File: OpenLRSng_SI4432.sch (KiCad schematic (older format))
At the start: 36 parts, among them IC1 ATMEGA328P-A, IC2 Si4432, P1 CONN_01X06, P2 CONN_02X09, P3 MML, U1 MIC5205 3,3V, Y1 RESONATEUR

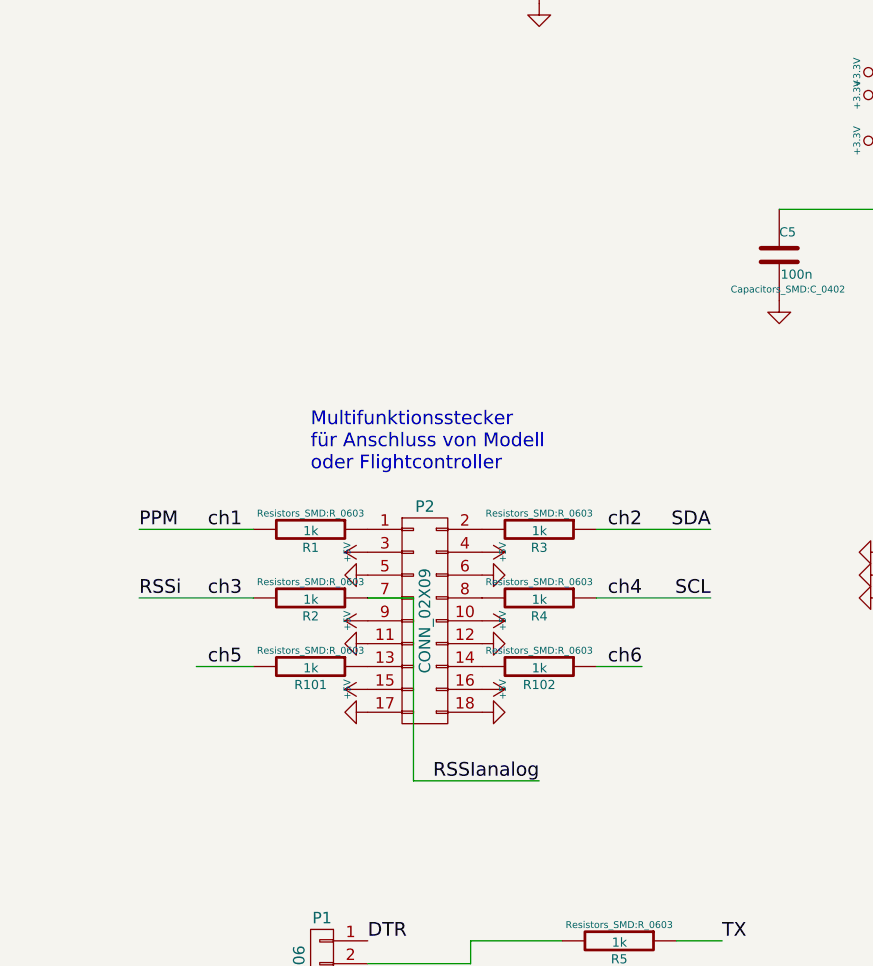
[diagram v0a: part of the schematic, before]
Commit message: Von 6 auf 4 Kanäle reduziert, I2C oder Analog in der Zusätzliche Kanäle über PicoBlade, Spannungsteiler/Pullup/Schutzwiderstandspads
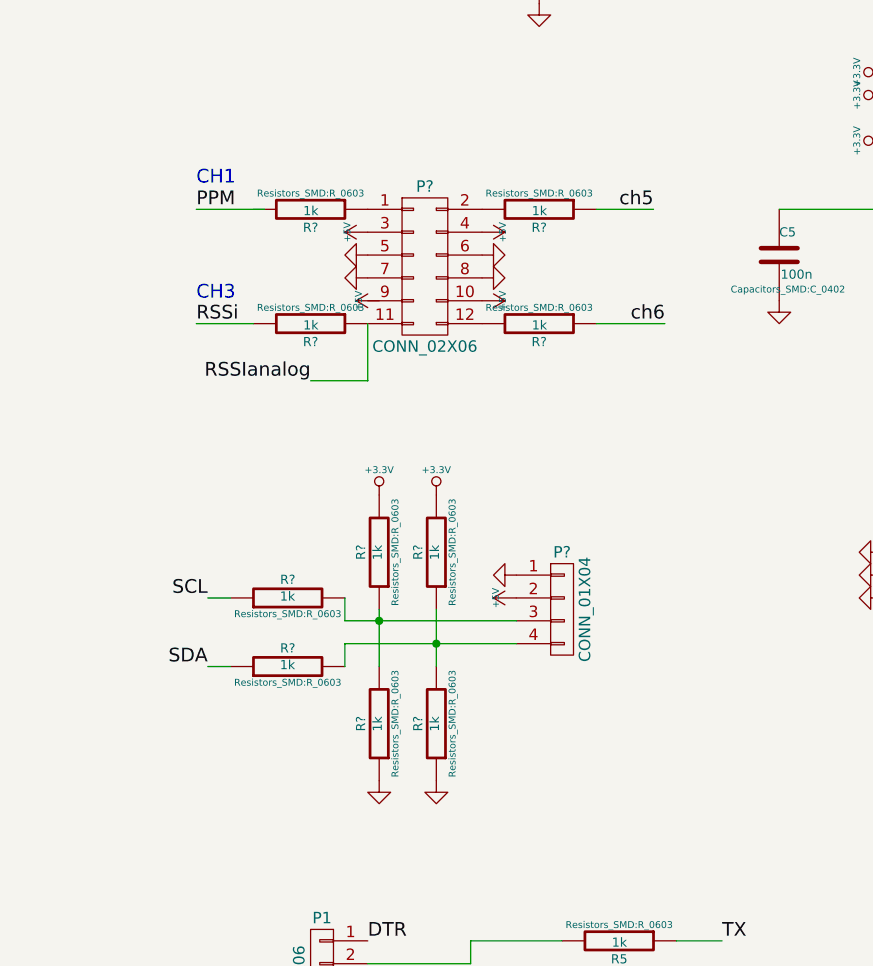
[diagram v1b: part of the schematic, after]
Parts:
- removed P2: CONN_02X09, Pin_Headers:Pin_Header_Angled_2x09, symbol CONN_02X09
- removed R1, R101, R102, R2, R3, R4: 1k, Resistors_SMD:R_0603, symbol R
- added P?: CONN_02X06, symbol CONN_02X06
- added P?: CONN_01X04, symbol CONN_01X04
- added R? (x10): 1k, Resistors_SMD:R_0603, symbol R
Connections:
- net +3.3V: now also R?.2, R?.2
- net +5V: now also P?.10 (P10), P?.2 (P2), P?.3 (P3), P?.4 (P4)
- net GND: now also P?.1 (P1), P?.5 (P5), P?.6 (P6), P?.7 (P7), P?.8 (P8), R?.1, R?.1
- net RSSIanalog: now also P?.11 (P11), R?.1
- net RSSi: now also R?.2
- net SCL: now also R?.1
- net SDA: now also R?.1
- net ch5: now also R?.1
- net ch6: now also R?.1
- new net: P?.1 (P1), R?.1
- new net: P?.12 (P12), R?.2
- new net: P?.2 (P2), R?.2
- new net: P?.3 (P3), R?.1, R?.2, R?.2
- new net: P?.4 (P4), R?.1, R?.2, R?.2
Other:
- note added: "CH1"
- note added: "CH3\n\n"
- note removed: "Multifunktionsstecker\nfür Anschluss von Modell\noder Flightcontroller"

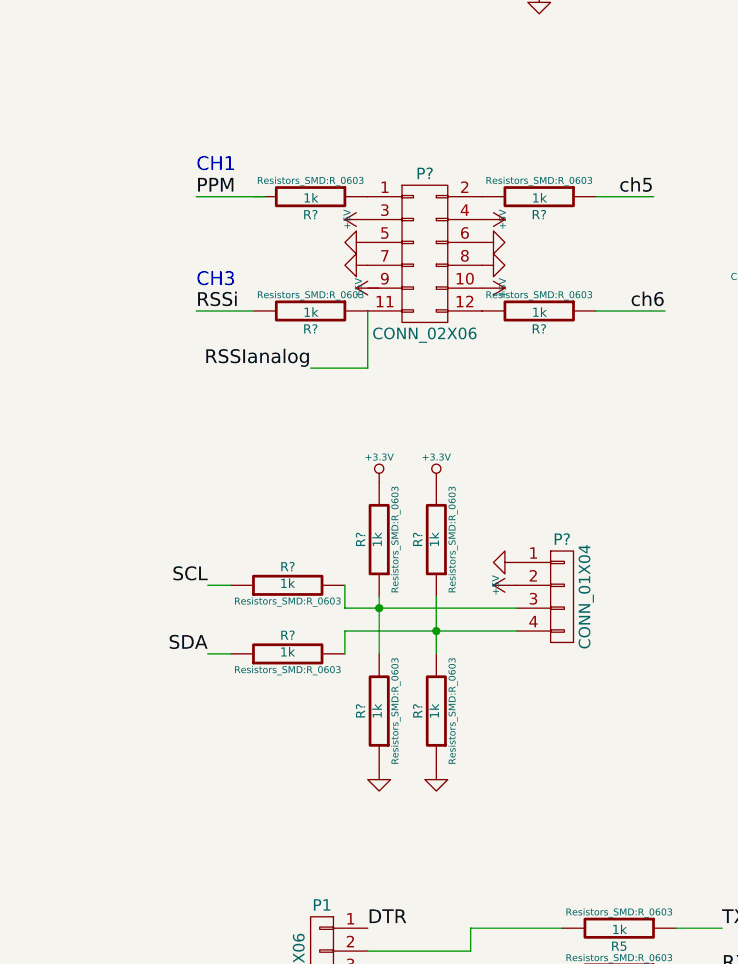
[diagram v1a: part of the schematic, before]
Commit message: Tiefpassfilter Cap an den Analog Inputs nachgerüstet
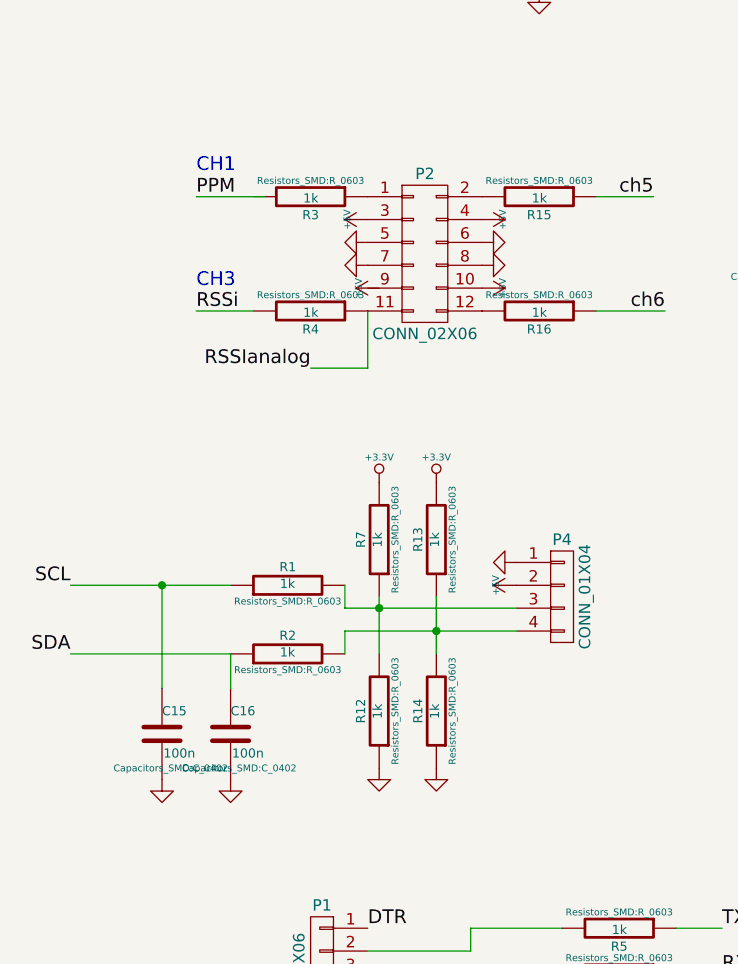
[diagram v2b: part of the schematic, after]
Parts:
- added C15, C16: 100n, Capacitors_SMD:C_0402, symbol C
- gave numbers to parts that had none: 12
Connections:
- net GND: now also C15.2, C16.2
- net SCL: now also C15.1
- net SDA: now also C16.1

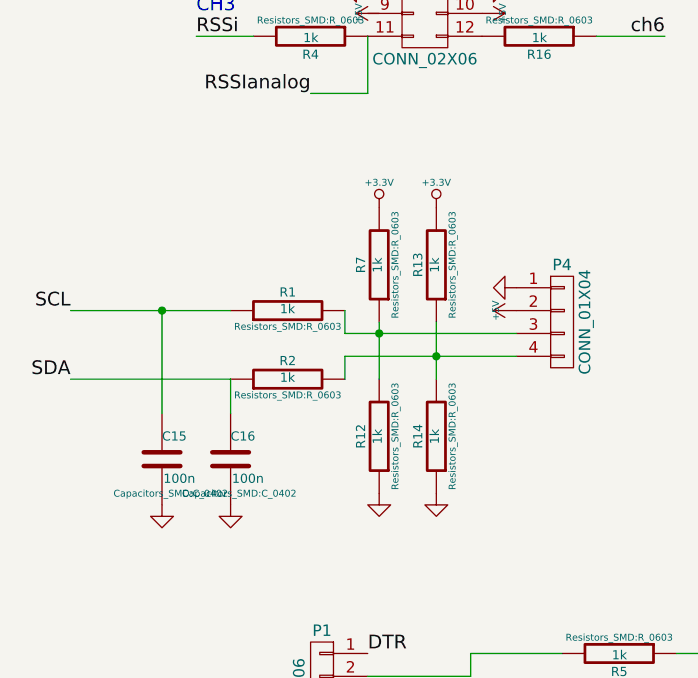
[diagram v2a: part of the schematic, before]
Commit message: Spannungsteiler korrigiert...
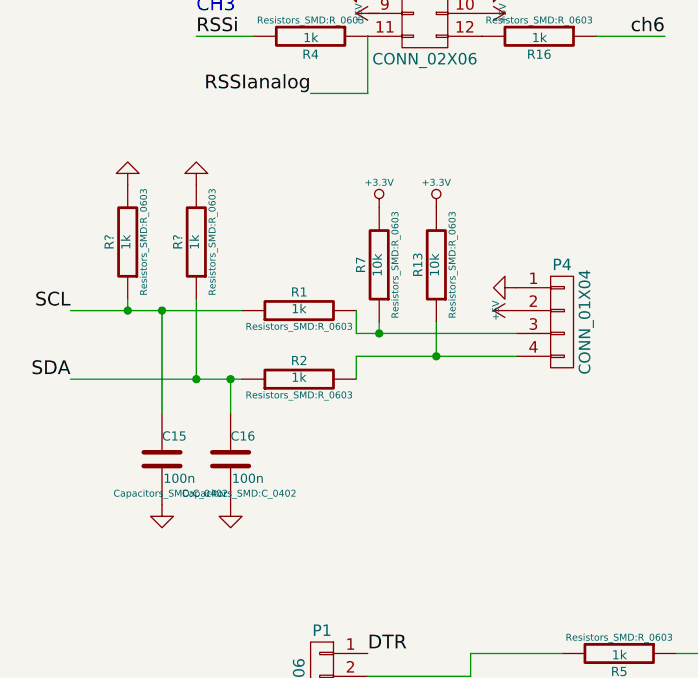
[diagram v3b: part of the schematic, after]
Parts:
- removed R12, R14: 1k, Resistors_SMD:R_0603, symbol R
- added R? (x2): 1k, Resistors_SMD:R_0603, symbol R
- R13, R7: value 1k -> 10k
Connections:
- net GND: now also R?.2, R?.2
- net SCL: now also R?.1
- net SDA: now also R?.1
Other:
- moved on the sheet: R1, R2
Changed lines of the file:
@@
 Text Label 850  5150 2    60   ~ 0
 SDA
-Wire Wire Line
-	2050 4950 2800 4950
-Wire Wire Line
-	2050 5050 2800 5050
 $Comp
 L R R13
@@
 P 2450 4650
 F 0 "R13" V 2530 4650 40  0000 C CNN
-F 1 "1k" V 2457 4651 40  0000 C CNN
+F 1 "10k" V 2457 4651 40  0000 C CNN
 F 2 "Resistors_SMD:R_0603" V 2380 4650 30  0000 C CNN
 F 3 "" H 2450 4650 30  0000 C CNN
@@
 	-1   0    0    1
 $EndComp
-$Comp
-L R R7
-U 1 1 54ED061F
-P 2200 4650
-F 0 "R7" V 2280 4650 40  0000 C CNN
-F 1 "1k" V 2207 4651 40  0000 C CNN
-F 2 "Resistors_SMD:R_0603" V 2130 4650 30  0000 C CNN
-F 3 "" H 2200 4650 30  0000 C CNN
-	1    2200 4650
-	-1   0    0    1
-$EndComp
-Wire Wire Line
-	2200 4900 2200 5150
-Connection ~ 2200 4950
-Wire Wire Line
-	2450 4900 2450 5150
 Connection ~ 2450 5050
-$Comp
-L +3.3V #PWR14
-U 1 1 54ED0C0E
-P 2200 4400
-F 0 "#PWR14" H 2200 4360 30  0001 C CNN
-F 1 "+3.3V" H 2200 4510 30  0000 C CNN
-F 2 "" H 2200 4400 60  0000 C CNN
-F 3 "" H 2200 4400 60  0000 C CNN
-	1    2200 4400
-	1    0    0    -1
-$EndComp
 $Comp
 L +3.3V #PWR16
@@
 L R R1
 U 1 1 54ED13EB
-P 1800 4850
-F 0 "R1" V 1880 4850 40  0000 C CNN
-F 1 "1k" V 1807 4851 40  0000 C CNN
-F 2 "Resistors_SMD:R_0603" V 1730 4850 30  0000 C CNN
-F 3 "" H 1800 4850 30  0000 C CNN
-	1    1800 4850
+P 1850 4850
+F 0 "R1" V 1930 4850 40  0000 C CNN
+F 1 "1k" V 1857 4851 40  0000 C CNN
+F 2 "Resistors_SMD:R_0603" V 1780 4850 30  0000 C CNN
+F 3 "" H 1850 4850 30  0000 C CNN
+	1    1850 4850
 	0    -1   -1   0
 $EndComp
@@
 L R R2
 U 1 1 54ED1487
-P 1800 5150
-F 0 "R2" V 1880 5150 40  0000 C CNN
-F 1 "1k" V 1807 5151 40  0000 C CNN
-F 2 "Resistors_SMD:R_0603" V 1730 5150 30  0000 C CNN
-F 3 "" H 1800 5150 30  0000 C CNN
-	1    1800 5150
+P 1850 5150
+F 0 "R2" V 1930 5150 40  0000 C CNN
+F 1 "1k" V 1857 5151 40  0000 C CNN
+F 2 "Resistors_SMD:R_0603" V 1780 5150 30  0000 C CNN
+F 3 "" H 1850 5150 30  0000 C CNN
+	1    1850 5150
 	0    -1   -1   0
 $EndComp
 Wire Wire Line
-	2050 4950 2050 4850
-Wire Wire Line
-	2050 5050 2050 5150
-$Comp
-L R R12
-U 1 1 54ED1B22
-P 2200 5400
-F 0 "R12" V 2280 5400 40  0000 C CNN
-F 1 "1k" V 2207 5401 40  0000 C CNN
-F 2 "Resistors_SMD:R_0603" V 2130 5400 30  0000 C CNN
-F 3 "" H 2200 5400 30  0000 C CNN
-	1    2200 5400
-	-1   0    0    1
-$EndComp
-$Comp
-L R R14
-U 1 1 54ED1B95
-P 2450 5400
-F 0 "R14" V 2530 5400 40  0000 C CNN
-F 1 "1k" V 2457 5401 40  0000 C CNN
-F 2 "Resistors_SMD:R_0603" V 2380 5400 30  0000 C CNN
-F 3 "" H 2450 5400 30  0000 C CNN
-	1    2450 5400
-	-1   0    0    1
-$EndComp
-Wire Wire Line
-	850  4850 1550 4850
-$Comp
-L GND #PWR15
-U 1 1 54ED1E5C
-P 2200 5650
-F 0 "#PWR15" H 2200 5650 30  0001 C CNN
-F 1 "GND" H 2200 5580 30  0001 C CNN
-F 2 "" H 2200 5650 60  0000 C CNN
-F 3 "" H 2200 5650 60  0000 C CNN
-	1    2200 5650
-	1    0    0    -1
-$EndComp
-$Comp
-L GND #PWR17
-U 1 1 54ED1E97
-P 2450 5650
-F 0 "#PWR17" H 2450 5650 30  0001 C CNN
-F 1 "GND" H 2450 5580 30  0001 C CNN
-F 2 "" H 2450 5650 60  0000 C CNN
-F 3 "" H 2450 5650 60  0000 C CNN
-	1    2450 5650
-	1    0    0    -1
-$EndComp
+	850  4850 1600 4850
 Text Notes 1400 3050 0    60   ~ 0
 CH1
@@
 Connection ~ 1250 4850
 Wire Wire Line
-	850  5150 1550 5150
+	850  5150 1600 5150
 $Comp
 L GND #PWR5
@@
 	1    0    0    -1
 $EndComp
+Connection ~ 2200 4950
+$Comp
+L +3.3V #PWR14
+U 1 1 54ED0C0E
+P 2200 4400
+F 0 "#PWR14" H 2200 4360 30  0001 C CNN
+F 1 "+3.3V" H 2200 4510 30  0000 C CNN
+F 2 "" H 2200 4400 60  0000 C CNN
+F 3 "" H 2200 4400 60  0000 C CNN
+	1    2200 4400
+	1    0    0    -1
+$EndComp
+$Comp
+L R R7
+U 1 1 54ED061F
+P 2200 4650
+F 0 "R7" V 2280 4650 40  0000 C CNN
+F 1 "10k" V 2207 4651 40  0000 C CNN
+F 2 "Resistors_SMD:R_0603" V 2130 4650 30  0000 C CNN
+F 3 "" H 2200 4650 30  0000 C CNN
+	1    2200 4650
+	-1   0    0    1
+$EndComp
+Wire Wire Line
+	2200 4950 2200 4900
+Wire Wire Line
+	2450 5050 2450 4900
+Wire Wire Line
+	2100 4850 2100 4950
+Wire Wire Line
+	2100 4950 2800 4950
+Wire Wire Line
+	2100 5050 2800 5050
+Wire Wire Line
+	2100 5050 2100 5150
+$Comp
+L R R?
+U 1 1 54ED67D4
+P 1400 4550
+F 0 "R?" V 1480 4550 40  0000 C CNN
+F 1 "1k" V 1407 4551 40  0000 C CNN
+F 2 "Resistors_SMD:R_0603" V 1330 4550 30  0000 C CNN
+F 3 "" H 1400 4550 30  0000 C CNN
+	1    1400 4550
+	-1   0    0    1
+$EndComp
+$Comp
+L R R?
+U 1 1 54ED684C
+P 1100 4550
+F 0 "R?" V 1180 4550 40  0000 C CNN
+F 1 "1k" V 1107 4551 40  0000 C CNN
+F 2 "Resistors_SMD:R_0603" V 1030 4550 30  0000 C CNN
+F 3 "" H 1100 4550 30  0000 C CNN
+	1    1100 4550
+	-1   0    0    1
+$EndComp
+Connection ~ 1550 5150
+$Comp
+L GND #PWR?
+U 1 1 54ED6A97
+P 1400 4300
+F 0 "#PWR?" H 1400 4300 30  0001 C CNN
+F 1 "GND" H 1400 4230 30  0001 C CNN
+F 2 "" H 1400 4300 60  0000 C CNN
+F 3 "" H 1400 4300 60  0000 C CNN
+	1    1400 4300
+	-1   0    0    1
+$EndComp
+$Comp
+L GND #PWR?
+U 1 1 54ED6ACD
+P 1100 4300
+F 0 "#PWR?" H 1100 4300 30  0001 C CNN
+F 1 "GND" H 1100 4230 30  0001 C CNN
+F 2 "" H 1100 4300 60  0000 C CNN
+F 3 "" H 1100 4300 60  0000 C CNN
+	1    1100 4300
+	-1   0    0    1
+$EndComp
+Wire Wire Line
+	1400 4800 1400 5150
+Connection ~ 1400 5150
+Wire Wire Line
+	1100 4800 1100 4850
+Connection ~ 1100 4850
 $EndSCHEMATC

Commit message: Schaltplan finalisiert, I²C-Stecker nach APM-Standard angebracht
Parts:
- P2: footprint (none) -> Pin_Headers:Pin_Header_Angled_2x09
- R12, R14: renamed from R?; value 1k -> *k
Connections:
- net +5V: now also P2.9 (P9)
- net PPM: now also R3.2
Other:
- note added: "Pullups I²C: R7 und R13 (immer bestückt)\nGlättungscaps: C15 und C16 (evtl. entfernen)\nSpannungsteiler: R12 und R14 (bestücken für U-Telemetrie\ndann: Pullups R7 und R13 entfernen!"
- note removed: "CH1"
- note removed: "CH3\n\n"
- moved on the sheet: C1, C10, C11, C12, C13, C14, C15, C16, C2, C3, C4, C5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

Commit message: picoblade dazu und layout etwas weiter. noch unfertig.
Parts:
- P4: footprint (none) -> Connectors_Molex:Connector_Molex_PicoBlade_53398-0471
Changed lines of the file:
@@
 F 0 "P4" H 3550 5050 50  0000 C CNN
 F 1 "CONN_01X04" V 3650 4800 50  0000 C CNN
-F 2 "" H 3550 4800 60  0001 C CNN
+F 2 "Connectors_Molex:Connector_Molex_PicoBlade_53398-0471" H 3550 4800 60  0001 C CNN
 F 3 "" H 3550 4800 60  0000 C CNN
 	1    3550 4800

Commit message: I²C Stecker im APM-Layout dazugefügt und Layout soweit fertig gemacht
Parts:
- P2: footprint Pin_Headers:Pin_Header_Angled_2x09 -> Pin_Headers:Pin_Header_Angled_2x06
- P4: footprint Connectors_Molex:Connector_Molex_PicoBlade_53398-0471 -> Connectors_Molex:Connector_Molex_PicoBlade_53261-0471
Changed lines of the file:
@@
 F 0 "P2" H 2550 3750 50  0000 C CNN
 F 1 "CONN_02X06" H 2550 3050 50  0000 C CNN
-F 2 "Pin_Headers:Pin_Header_Angled_2x09" H 2550 2200 60  0001 C CNN
+F 2 "Pin_Headers:Pin_Header_Angled_2x06" H 2550 2200 60  0001 C CNN
 F 3 "" H 2550 2200 60  0000 C CNN
 	1    2550 3400
@@
 F 0 "P4" H 3550 5050 50  0000 C CNN
 F 1 "CONN_01X04" V 3650 4800 50  0000 C CNN
-F 2 "Connectors_Molex:Connector_Molex_PicoBlade_53398-0471" H 3550 4800 60  0001 C CNN
+F 2 "Connectors_Molex:Connector_Molex_PicoBlade_53261-0471" H 3550 4800 60  0001 C CNN
 F 3 "" H 3550 4800 60  0000 C CNN
 	1    3550 4800
